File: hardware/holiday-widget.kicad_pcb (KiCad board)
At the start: 4 copper layers, 150 x 75 mm, 117 parts, among them J2 UART, J33 Conn_02x05_Odd_Even, J4 BATTERY POWER, J5 VDC POWER, J7 Speaker, Q1 MMBT3906, Q2 MMBT3906, Q3 MMBT3906, Q4 MMBT3906, Q5 MMBT3906, Q6 MMBT3906, Q7 MMBT3906, Q8 MMBT3906, SW1 SW_Push, SW4 SW_Push, U1 STM32L072RBTx, U2 TPS61200DRC, U3 LIS3DH, U4 IMP23ABSU, U6 VCNL_4020, U7 PAM8302AAD, U8 OPA355NA

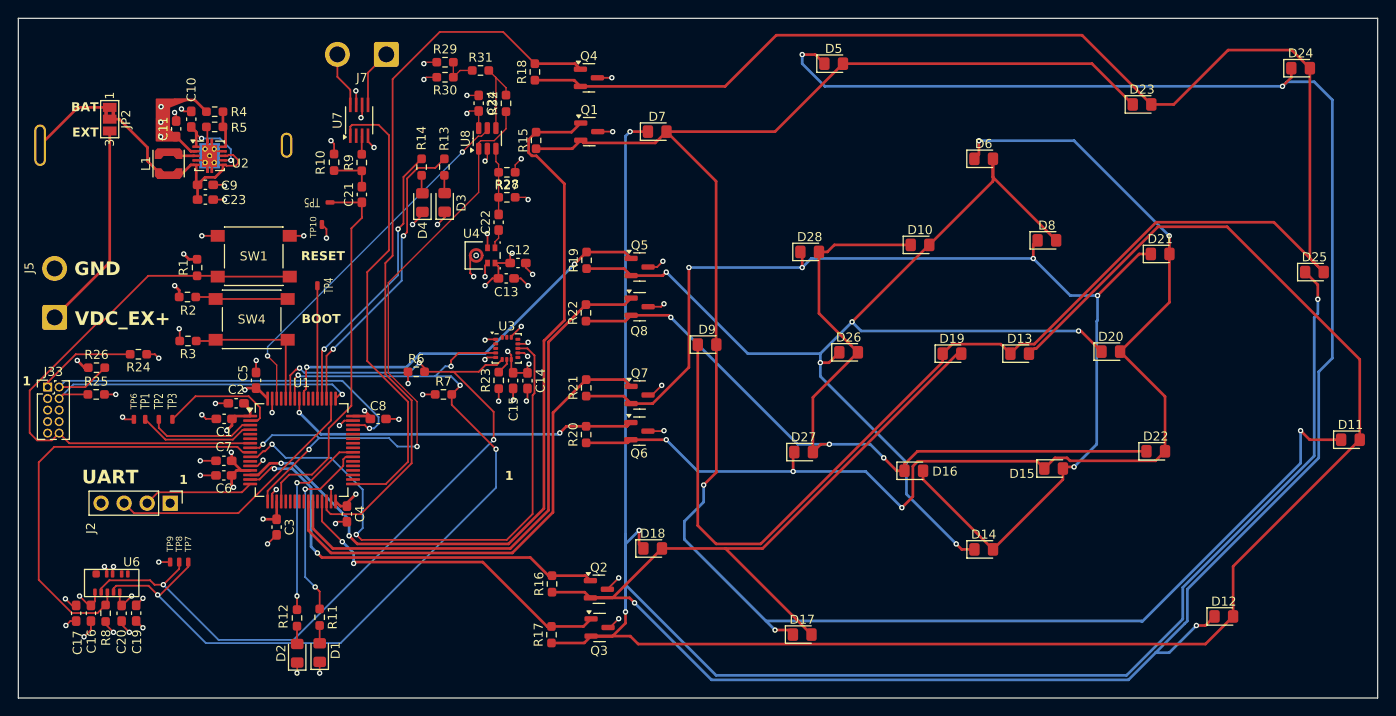
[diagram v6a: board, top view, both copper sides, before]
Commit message: [Hardware] Update LEDs
Add additional LEDs and arrange in 7x7 matrix. Remove 2x status LEDs. Reroute MCU connetions to be more sensible. Rearrange components.
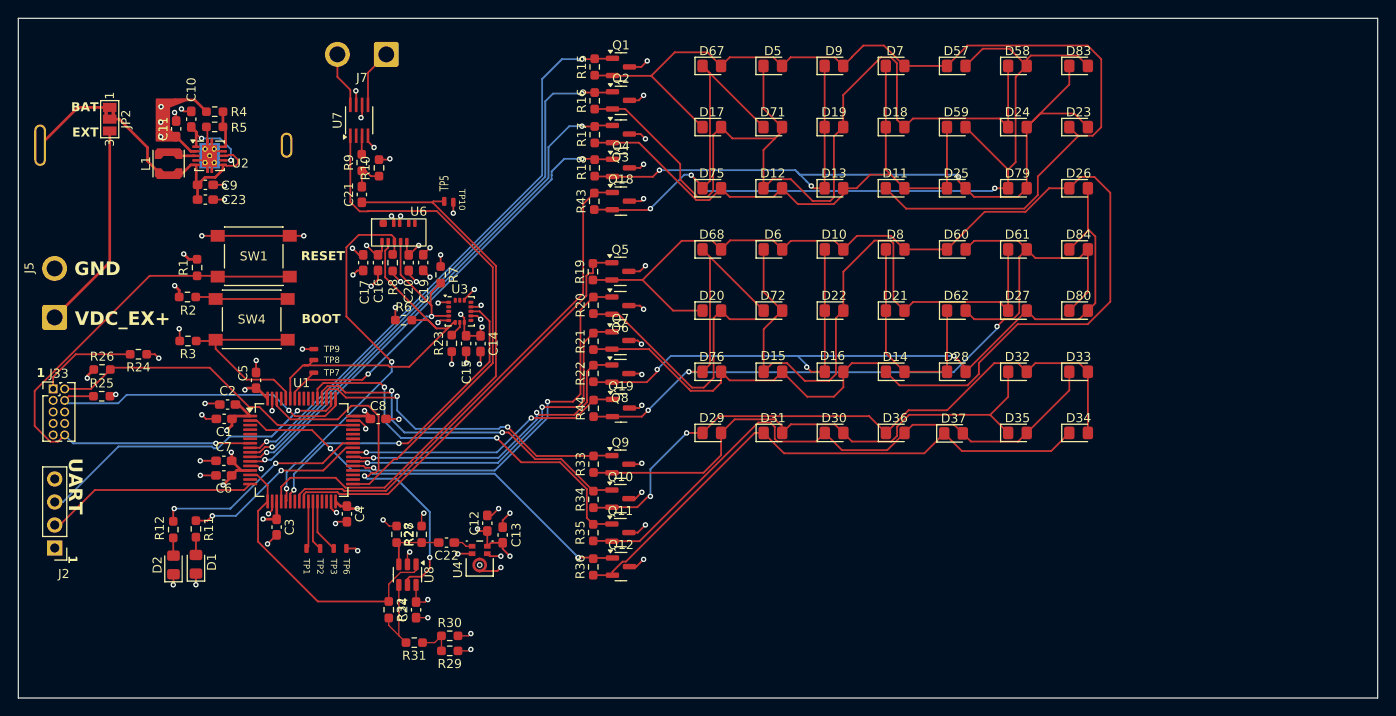
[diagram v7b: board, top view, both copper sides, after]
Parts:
- removed D3, D4: LED, LED_SMD:LED_0805_2012Metric_Pad1.15x1.40mm_HandSolder
- removed R13, R14: 120, Resistor_SMD:R_0603_1608Metric_Pad0.98x0.95mm_HandSolder
- removed TP4: TestPoint, Leaf_Jumper:TestPoint_0.5mm_1mm
- added D29: LED, LED_SMD:LED_0805_2012Metric_Pad1.15x1.40mm_HandSolder, F.Cu at (190.5, 117.2)
- added D30: LED, LED_SMD:LED_0805_2012Metric_Pad1.15x1.40mm_HandSolder, F.Cu at (204.0, 117.2)
- added D31: LED, LED_SMD:LED_0805_2012Metric_Pad1.15x1.40mm_HandSolder, F.Cu at (197.3, 117.2)
- added D32: LED, LED_SMD:LED_0805_2012Metric_Pad1.15x1.40mm_HandSolder, F.Cu at (224.3, 110.5)
- added D33: LED, LED_SMD:LED_0805_2012Metric_Pad1.15x1.40mm_HandSolder, F.Cu at (231.0, 110.5)
- added D34: LED, LED_SMD:LED_0805_2012Metric_Pad1.15x1.40mm_HandSolder, F.Cu at (231.0, 117.2)
- added D35: LED, LED_SMD:LED_0805_2012Metric_Pad1.15x1.40mm_HandSolder, F.Cu at (224.3, 117.2)
- added D36: LED, LED_SMD:LED_0805_2012Metric_Pad1.15x1.40mm_HandSolder, F.Cu at (210.8, 117.2)
- added D37: LED, LED_SMD:LED_0805_2012Metric_Pad1.15x1.40mm_HandSolder, F.Cu at (217.2, 117.3)
- added D57: LED, LED_SMD:LED_0805_2012Metric_Pad1.15x1.40mm_HandSolder, F.Cu at (217.5, 76.8)
- added D58: LED, LED_SMD:LED_0805_2012Metric_Pad1.15x1.40mm_HandSolder, F.Cu at (224.2, 76.8)
- added D59: LED, LED_SMD:LED_0805_2012Metric_Pad1.15x1.40mm_HandSolder, F.Cu at (217.5, 83.5)
- added D60: LED, LED_SMD:LED_0805_2012Metric_Pad1.15x1.40mm_HandSolder, F.Cu at (217.5, 97.0)
- added D61: LED, LED_SMD:LED_0805_2012Metric_Pad1.15x1.40mm_HandSolder, F.Cu at (224.3, 97.0)
- added D62: LED, LED_SMD:LED_0805_2012Metric_Pad1.15x1.40mm_HandSolder, F.Cu at (217.5, 103.8)
- added D67: LED, LED_SMD:LED_0805_2012Metric_Pad1.15x1.40mm_HandSolder, F.Cu at (190.5, 76.8)
- added D68: LED, LED_SMD:LED_0805_2012Metric_Pad1.15x1.40mm_HandSolder, F.Cu at (190.5, 97.0)
- added D71: LED, LED_SMD:LED_0805_2012Metric_Pad1.15x1.40mm_HandSolder, F.Cu at (197.2, 83.5)
- added D72: LED, LED_SMD:LED_0805_2012Metric_Pad1.15x1.40mm_HandSolder, F.Cu at (197.3, 103.8)
- added D75: LED, LED_SMD:LED_0805_2012Metric_Pad1.15x1.40mm_HandSolder, F.Cu at (190.5, 90.2)
- added D76: LED, LED_SMD:LED_0805_2012Metric_Pad1.15x1.40mm_HandSolder, F.Cu at (190.5, 110.5)
- added D79: LED, LED_SMD:LED_0805_2012Metric_Pad1.15x1.40mm_HandSolder, F.Cu at (224.2, 90.2)
- added D80: LED, LED_SMD:LED_0805_2012Metric_Pad1.15x1.40mm_HandSolder, F.Cu at (231.0, 103.8)
- added D83: LED, LED_SMD:LED_0805_2012Metric_Pad1.15x1.40mm_HandSolder, F.Cu at (231.0, 76.8)
- added D84: LED, LED_SMD:LED_0805_2012Metric_Pad1.15x1.40mm_HandSolder, F.Cu at (231.0, 97.0)
- added Q10: MMBT3906, Package_TO_SOT_SMD:SOT-23, F.Cu at (180.4, 124.5)
- added Q11: MMBT3906, Package_TO_SOT_SMD:SOT-23, F.Cu at (180.4, 128.2)
- added Q12: MMBT3906, Package_TO_SOT_SMD:SOT-23, F.Cu at (180.5, 132.0)
- added Q18: MMBT3906, Package_TO_SOT_SMD:SOT-23, F.Cu at (180.5, 91.7)
- added Q19: MMBT3906, Package_TO_SOT_SMD:SOT-23, F.Cu at (180.5, 114.5)
- added Q9: MMBT3906, Package_TO_SOT_SMD:SOT-23, F.Cu at (180.4, 120.7)
- added R33: 50, Resistor_SMD:R_0603_1608Metric_Pad0.98x0.95mm_HandSolder, F.Cu at (177.5, 120.7)
- added R34: 50, Resistor_SMD:R_0603_1608Metric_Pad0.98x0.95mm_HandSolder, F.Cu at (177.5, 124.6)
- added R35: 50, Resistor_SMD:R_0603_1608Metric_Pad0.98x0.95mm_HandSolder, F.Cu at (177.4, 128.3)
- added R36: 50, Resistor_SMD:R_0603_1608Metric_Pad0.98x0.95mm_HandSolder, F.Cu at (177.4, 132.0)
- added R43: 50, Resistor_SMD:R_0603_1608Metric_Pad0.98x0.95mm_HandSolder, F.Cu at (177.6, 91.7)
- added R44: 50, Resistor_SMD:R_0603_1608Metric_Pad0.98x0.95mm_HandSolder, F.Cu at (177.5, 114.5)
- moved D12 68.6 mm to (197.2, 90.2)
- moved R29 65.0 mm to (161.6, 141.3), turned to 180 degrees
- moved R31 63.6 mm to (157.7, 140.4), turned to 180 degrees
- moved R30 61.6 mm to (161.6, 139.6), turned to 0 degrees
- moved D11 57.4 mm to (210.8, 90.2)
- moved R32 57.4 mm to (154.9, 136.8), turned to -90 degrees
- moved D17 56.9 mm to (190.5, 83.5)
- moved C24 56.3 mm to (157.9, 136.8), turned to 90 degrees
- moved R17 55.4 mm to (177.6, 84.3)
- moved Q3 54.5 mm to (180.5, 84.3)
- moved Q2 54.0 mm to (180.5, 80.6)
- moved D18 53.6 mm to (210.8, 83.5)
- moved R16 53.5 mm to (177.6, 80.6)
- moved C17 50.0 mm to (152.1, 98.5)
- moved C20 50.0 mm to (157.1, 98.5)
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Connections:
- Q5 pad 1: /mcu/LED4 -> /mcu/LED5
- Q6 pad 1: /mcu/LED5 -> /mcu/LED6
- Q7 pad 1: /mcu/LED6 -> /mcu/LED7
- Q8 pad 1: /mcu/LED7 -> /mcu/LED8
- R19 pad 2: /mcu/LED4 -> /mcu/LED5
- R20 pad 2: /mcu/LED5 -> /mcu/LED6
- R21 pad 2: /mcu/LED6 -> /mcu/LED7
- R22 pad 2: /mcu/LED7 -> /mcu/LED8
- TP1 pad 1: Net-(U1-PC15) -> Net-(U1-PB0)
- TP2 pad 1: Net-(U1-PC14) -> Net-(U1-PB1)
- TP3 pad 1: Net-(U1-PC13) -> Net-(U1-PB2)
- U1 pad 10: /Sensors/LIS3DH_INT -> /mcu/LED2
- U1 pad 11: unconnected-(U1-PC3-Pad11) -> /mcu/LED3
- U1 pad 14: /mcu/LED0 -> /Audio Amp/AUDIO_OUT
- U1 pad 15: /mcu/LED1 -> unconnected-(U1-PA1-Pad15)
- U1 pad 2: Net-(U1-PC13) -> /mcu/LED13
- U1 pad 21: unconnected-(U1-PA5-Pad21) -> /Sensors/VCNL4020_INT
- U1 pad 22: unconnected-(U1-PA6-Pad22) -> /Sensors/LIS3DH_INT
- U1 pad 24: unconnected-(U1-PC4-Pad24) -> /mcu/LED4
- U1 pad 25: unconnected-(U1-PC5-Pad25) -> /mcu/LED5
- U1 pad 26: /mcu/LED6 -> Net-(U1-PB0)
- U1 pad 27: /mcu/LED7 -> Net-(U1-PB1)
- U1 pad 28: unconnected-(U1-PB2-Pad28) -> Net-(U1-PB2)
- U1 pad 29: /mcu/LED2 -> unconnected-(U1-PB10-Pad29)
- U1 pad 3: Net-(U1-PC14) -> unconnected-(U1-PC14-Pad3)
- U1 pad 30: /mcu/LED3 -> unconnected-(U1-PB11-Pad30)
- U1 pad 37: unconnected-(U1-PC6-Pad37) -> /mcu/LED6
- U1 pad 38: unconnected-(U1-PC7-Pad38) -> /mcu/LED7
- U1 pad 39: /mcu/STAT_LED0 -> /mcu/LED8
- U1 pad 4: Net-(U1-PC15) -> unconnected-(U1-PC15-Pad4)
- U1 pad 40: /mcu/STAT_LED1 -> /mcu/LED9
- U1 pad 41: unconnected-(U1-PA8-Pad41) -> /mcu/STAT_LED0
- U1 pad 42: unconnected-(U1-PA9-Pad42) -> /mcu/STAT_LED1
- U1 pad 51: /mcu/STAT_LED2 -> /mcu/LED10
- U1 pad 52: /mcu/STAT_LED3 -> /mcu/LED11
- U1 pad 53: Net-(U1-PC12) -> /mcu/LED12
- U1 pad 56: /mcu/LED4 -> unconnected-(U1-PB4-Pad56)
- U1 pad 57: /mcu/LED5 -> unconnected-(U1-PB5-Pad57)
- U1 pad 8: /Audio Amp/AUDIO_OUT -> /mcu/LED0
- U1 pad 9: /Sensors/VCNL4020_INT -> /mcu/LED1
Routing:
- net /Input and Output/LED Output/CTRL2: track 351.1 -> 64.9 mm, vias 4 -> 0
- net /Input and Output/LED Output/CTRL1: track 281.5 -> 102.9 mm, vias 4 -> 0
- net /Input and Output/LED Output/CTRL3: track 226.0 -> 90.5 mm, vias 0 -> 3
- net /Input and Output/LED Output1/CTRL4: track 0.00 -> 111.6 mm, vias 0 -> 3
- net /Input and Output/LED Output/CTRL4: track 0.00 -> 111.3 mm, vias 0 -> 3
- net /Input and Output/LED Output/CTRL0: track 211.7 -> 109.2 mm, vias 3 -> 0
- net /Input and Output/LED Output2/CTRL1: track 0.00 -> 72.4 mm, vias 0 -> 2
- net /Input and Output/LED Output2/CTRL2: track 0.00 -> 67.1 mm
- net /I2C.SCL: track 100.5 -> 34.8 mm, vias 5 -> 2
- net /Input and Output/LED Output2/CTRL3: track 0.00 -> 62.7 mm
- net /Input and Output/LED Output1/CTRL2: track 128.6 -> 67.1 mm, vias 5 -> 0
- net /Input and Output/LED Output2/CTRL0: track 0.00 -> 60.1 mm
- net /I2C.SDA: track 97.0 -> 41.2 mm, vias 4 -> 0
- net /mcu/LED13: track 0.00 -> 46.3 mm, vias 0 -> 2
- net /mcu/LED12: track 0.00 -> 44.4 mm, vias 0 -> 2
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
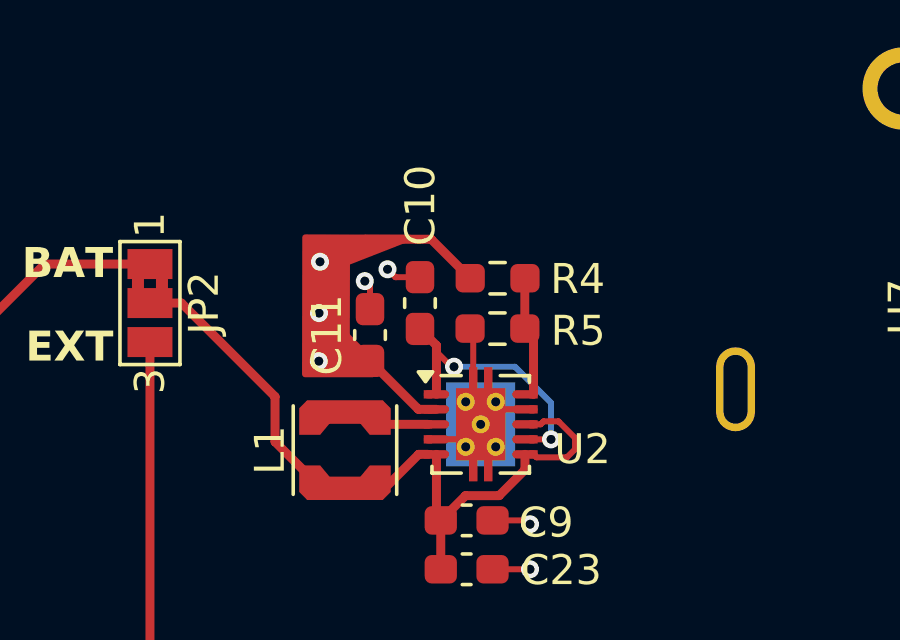
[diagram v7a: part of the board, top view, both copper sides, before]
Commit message: [Hardware] Boost converter updates.
* Tie PS (power save) pin to ground to enable higher efficiencies during low-current operation
* Add 0ohm resistor at output pin to measure current.
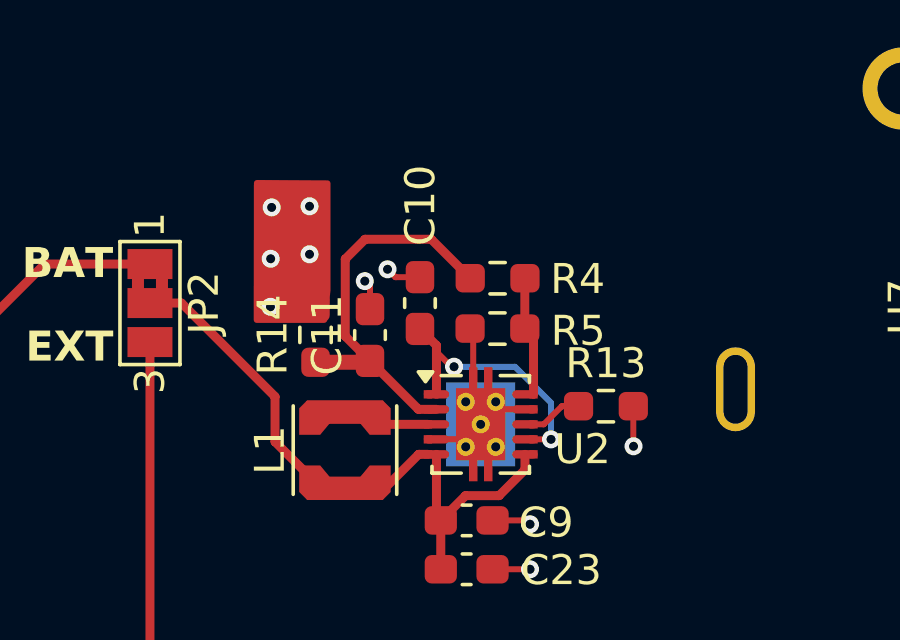
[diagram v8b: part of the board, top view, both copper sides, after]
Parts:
- added R13: 0, Resistor_SMD:R_0603_1608Metric_Pad0.98x0.95mm_HandSolder, F.Cu at (139.3, 86.1)
- added R14: 0, Resistor_SMD:R_0603_1608Metric_Pad0.98x0.95mm_HandSolder, F.Cu at (129.6, 83.7)
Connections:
- C11 pad 1: /VDD -> Net-(U2-VOUT)
- R4 pad 1: /VDD -> Net-(U2-VOUT)
- U2 pad 2: /VDD -> Net-(U2-VOUT)
- U2 pad 8: Net-(JP2-C) -> Net-(U2-PS)
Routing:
- net Net-(U2-VOUT): track 0.00 -> 13.4 mm
- net /VDD: track 78.9 -> 67.3 mm, vias 31 -> 33
- net Net-(JP2-C): track 24.3 -> 20.7 mm
- net Net-(U2-PS): track 0.00 -> 2.04 mm
- net /GND: track 108.4 -> 109.7 mm, vias 64 -> 65
